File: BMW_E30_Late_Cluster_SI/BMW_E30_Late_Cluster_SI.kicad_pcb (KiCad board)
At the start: 2 copper layers, 300 x 53 mm, 115 parts, among them J1 SI LED Board, J2 Coding Plug, J5 Nexus Connector, Q11 BC327-16, Q12 BC337-25, Q13 BC337-16, Q14 BC547B, Q15 BC557B, Q17 BC337-25, Q19 BC337-25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

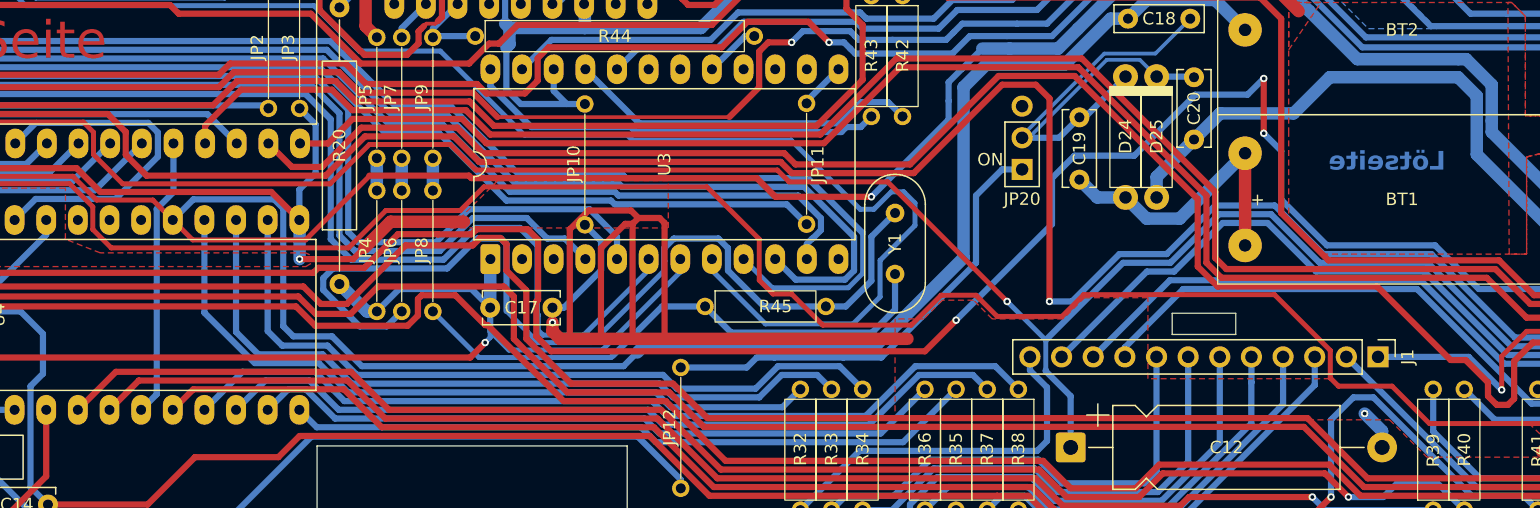
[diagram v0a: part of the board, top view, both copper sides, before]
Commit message: Readability Improvements
Organized the schematic for better readability, also made a few minor adjustments to the layout for simplicity.
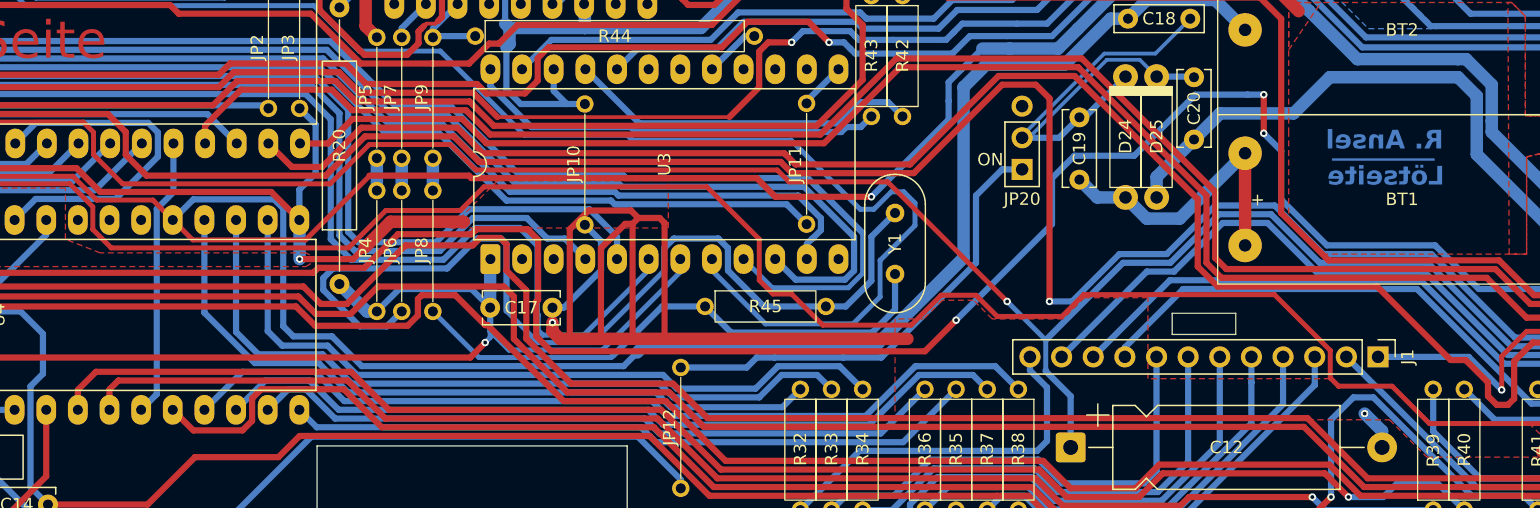
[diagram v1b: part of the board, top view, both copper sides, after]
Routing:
- net IC4_P16: track 126.0 -> 128.4 mm
- net IC4_P40: track 227.8 -> 226.0 mm
- net IC4_P14: track 112.1 -> 113.1 mm
- net IC4_P13: track 119.8 -> 120.8 mm
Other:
- board text added: "R. Ansel"
- board text added: "________"
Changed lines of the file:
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@@
 	(title_block
 		(title "BMW E30 Late Model SI Board")
+		(date "2025-12-07")
 		(rev "0")
 		(company "Reagan Ansel")
@@
 		(tags "Resistor Axial_DIN0204 series Axial Horizontal pin pitch 7.62mm 0.167W length 3.6mm diameter 1.6mm")
 		(property "Reference" "JP11"
-			(at 4.9 -0.9 90)
+			(at 4.9 0.9 90)
 			(layer "F.SilkS")
 			(effects
@@
 		(tags "Resistor Axial_DIN0204 series Axial Horizontal pin pitch 7.62mm 0.167W length 3.6mm diameter 1.6mm")
 		(property "Reference" "R45"
-			(at 5.65 0 0)
+			(at 4.85 0 0)
 			(layer "F.SilkS")
 			(effects
@@
 	)
 	(gr_text "Lötseite"
-		(at 240 153.7 0)
+		(at 235.2 154.9 0)
 		(layer "B.Cu")
 		(effects
@@
 				(bold yes)
 			)
-			(justify left bottom mirror)
+			(justify bottom mirror)
+		)
+	)
+	(gr_text "R. Ansel"
+		(at 235.1 152 0)
+		(layer "B.Cu")
+		(effects
+			(font
+				(size 1.5 1.5)
+				(thickness 0.3)
+				(bold yes)
+			)
+			(justify bottom mirror)
+		)
+	)
+	(gr_text "________"
+		(at 235 152.5 0)
+		(layer "B.Cu")
+		(effects
+			(font
+				(size 1.5 1.5)
+				(thickness 0.3)
+				(bold yes)
+			)
+			(justify bottom mirror)
 		)
 	)
@@
 	)
 	(segment
-		(start 225.4 150.6)
-		(end 225.4 146.2)
-		(width 0.5)
-		(layer "F.Cu")
-		(net 27)
-	)
-	(segment
 		(start 200.7 165.6)
 		(end 198.2 168.1)
@@
 	)
 	(segment
+		(start 225.4 150.6)
+		(end 225.4 147.5)
+		(width 0.5)
+		(layer "F.Cu")
+		(net 27)
+	)
+	(segment
 		(start 96.1 159.3)
 		(end 97.84 157.56)
@@
 	)
 	(via
-		(at 225.4 146.2)
+		(at 225.4 147.5)
 		(size 0.6)
 		(drill 0.3)
@@
 	)
 	(segment
-		(start 210.2 152.4)
-		(end 215 152.4)
+		(start 224.099 147.501)
+		(end 219.899 147.501)
 		(width 0.5)
 		(layer "B.Cu")
@@
 	)
 	(segment
+		(start 208.4 154.2)
+		(end 208.4 157.9)
+		(width 0.5)
+		(layer "B.Cu")
+		(net 27)
+	)
+	(segment
 		(start 270.6 157.7)
 		(end 268.7 159.6)
@@
 	)
 	(segment
+		(start 225.4 147.5)
+		(end 224.1 147.5)
+		(width 0.5)
+		(layer "B.Cu")
+		(net 27)
+	)
+	(segment
 		(start 273.1 154.55)
 		(end 273.1 157.9)
@@
 	)
 	(segment
-		(start 226.8 155.925908)
-		(end 226.8 152)
+		(start 210.2 152.4)
+		(end 208.4 154.2)
 		(width 0.5)
 		(layer "B.Cu")
@@
 	)
 	(segment
-		(start 257.7 163.1)
-		(end 242.65682 163.1)
+		(start 226.8 155.925908)
+		(end 226.8 152)
 		(width 0.5)
 		(layer "B.Cu")
@@
 	)
 	(segment
-		(start 208.4 154.2)
-		(end 210.2 152.4)
+		(start 257.7 163.1)
+		(end 242.65682 163.1)
 		(width 0.5)
 		(layer "B.Cu")
@@
 	)
 	(segment
-		(start 219.899 147.501)
-		(end 224.099 147.501)
+		(start 215 152.4)
+		(end 210.2 152.4)
 		(width 0.5)
 		(layer "B.Cu")
@@
 	)
 	(segment
-		(start 215 152.4)
-		(end 219.899 147.501)
-		(width 0.5)
+		(start 273.1 157.9)
+		(end 274 158.8)
+		(width 1)
 		(layer "B.Cu")
 		(net 27)
 	)
 	(segment
-		(start 208.4 157.9)
-		(end 208.4 154.2)
+		(start 219.899 147.501)
+		(end 215 152.4)
 		(width 0.5)
 		(layer "B.Cu")
@@
 	)
 	(segment
-		(start 273.1 157.9)
-		(end 274 158.8)
-		(width 1)
-		(layer "B.Cu")
-		(net 27)
-	)
-	(segment
-		(start 224.099 147.501)
-		(end 225.4 146.2)
+		(start 208.4 157.9)
+		(end 200.7 165.6)
 		(width 0.5)
 		(layer "B.Cu")
@@
 	)
 	(segment
-		(start 200.7 165.6)
-		(end 208.4 157.9)
+		(start 224.1 147.5)
+		(end 224.099 147.501)
 		(width 0.5)
 		(layer "B.Cu")
@@
 	(segment
 		(start 151.839364 170.448)
-		(end 135.092 170.448)
+		(end 133.452 170.448)
 		(width 0.5)
 		(layer "F.Cu")
@@
 	)
 	(segment
-		(start 209.282728 180.5)
-		(end 207.079728 178.297)
+		(start 229.3 179.8)
+		(end 219.4 179.8)
 		(width 0.5)
 		(layer "F.Cu")
@@
 	)
 	(segment
-		(start 176.736046 173.499)
-		(end 154.890364 173.499)
+		(start 207.079728 178.297)
+		(end 181.534046 178.297)
 		(width 0.5)
 		(layer "F.Cu")
@@
 	)
 	(segment
-		(start 207.079728 178.297)
-		(end 181.534046 178.297)
+		(start 132.74 171.16)
+		(end 132.74 172.8)
 		(width 0.5)
 		(layer "F.Cu")
@@
 	)
 	(segment
-		(start 219.4 179.8)
-		(end 218.7 180.5)
+		(start 181.534046 178.297)
+		(end 176.736046 173.499)
 		(width 0.5)
 		(layer "F.Cu")
@@
 	)
 	(segment
-		(start 229.3 179.8)
-		(end 219.4 179.8)
+		(start 209.282728 180.5)
+		(end 207.079728 178.297)
 		(width 0.5)
 		(layer "F.Cu")
@@
 	)
 	(segment
-		(start 181.534046 178.297)
-		(end 176.736046 173.499)
+		(start 176.736046 173.499)
+		(end 154.890364 173.499)
 		(width 0.5)
 		(layer "F.Cu")
@@
 	)
 	(segment
-		(start 135.092 170.448)
-		(end 132.74 172.8)
+		(start 133.452 170.448)
+		(end 132.74 171.16)
+		(width 0.5)
+		(layer "F.Cu")
+		(net 78)
+	)
+	(segment
+		(start 219.4 179.8)
+		(end 218.7 180.5)
 		(width 0.5)
 		(layer "F.Cu")
@@
 	)
 	(segment
-		(start 217.299 177.9)
-		(end 215.4 179.799)
+		(start 209.573092 179.799)
+		(end 207.370092 177.596)
 		(width 0.5)
 		(layer "F.Cu")
@@
 	)
 	(segment
-		(start 207.370092 177.596)
-		(end 181.82441 177.596)
+		(start 230.3 177.9)
+		(end 217.299 177.9)
 		(width 0.5)
 		(layer "F.Cu")
@@
 	)
 	(segment
-		(start 230.3 177.9)
-		(end 217.299 177.9)
+		(start 181.82441 177.596)
+		(end 177.02641 172.798)
 		(width 0.5)
 		(layer "F.Cu")
@@
 	)
 	(segment
-		(start 177.02641 172.798)
-		(end 155.180728 172.798)
+		(start 155.180728 172.798)
+		(end 152.129728 169.747)
 		(width 0.5)
 		(layer "F.Cu")
@@
 	)
 	(segment
-		(start 133.253 169.747)
-		(end 130.2 172.8)
+		(start 207.370092 177.596)
+		(end 181.82441 177.596)
 		(width 0.5)
 		(layer "F.Cu")
@@
 	)
 	(segment
-		(start 181.82441 177.596)
-		(end 177.02641 172.798)
+		(start 152.129728 169.747)
+		(end 131.653 169.747)
 		(width 0.5)
 		(layer "F.Cu")
@@
 	)
 	(segment
-		(start 155.180728 172.798)
-		(end 152.129728 169.747)
+		(start 177.02641 172.798)
+		(end 155.180728 172.798)
 		(width 0.5)
 		(layer "F.Cu")
@@
 	)
 	(segment
-		(start 209.573092 179.799)
-		(end 207.370092 177.596)
+		(start 131.653 169.747)
+		(end 130.2 171.2)
 		(width 0.5)
 		(layer "F.Cu")
@@
 	)
 	(segment
-		(start 152.129728 169.747)
-		(end 133.253 169.747)
+		(start 130.2 171.2)
+		(end 130.2 172.8)
+		(width 0.5)
+		(layer "F.Cu")
+		(net 79)
+	)
+	(segment
+		(start 217.299 177.9)
+		(end 215.4 179.799)
 		(width 0.5)
 		(layer "F.Cu")
@@
 	)
 	(segment
-		(start 139.471 171.149)
+		(start 139.471 174.451)
 		(end 137.82 172.8)
 		(width 0.5)
@@
 	)
 	(segment
-		(start 176.445682 174.2)
-		(end 154.6 174.2)
+		(start 154.6 174.2)
+		(end 151.549 171.149)
 		(width 0.5)
 		(layer "F.Cu")
@@
 	)
 	(segment
-		(start 154.6 174.2)
-		(end 151.549 171.149)
+		(start 181.243682 178.998)
+		(end 176.445682 174.2)
 		(width 0.5)
 		(layer "F.Cu")
@@
 	)
 	(segment
-		(start 151.549 171.149)
-		(end 139.471 171.149)
+		(start 176.445682 174.2)
+		(end 154.6 174.2)
 		(width 0.5)
 		(layer "F.Cu")
@@
 	)
 	(segment
-		(start 206.789364 178.998)
-		(end 181.243682 178.998)
+		(start 144.921819 171.149)
+		(end 144.189 171.881819)
 		(width 0.5)
 		(layer "F.Cu")
@@
 	)
 	(segment
-		(start 230.8 179.8)
-		(end 229.052 181.548)
+		(start 229.052 181.548)
+		(end 209.339364 181.548)
 		(width 0.5)
 		(layer "F.Cu")
@@
 	)
 	(segment
-		(start 229.052 181.548)
-		(end 209.339364 181.548)
+		(start 144.189 171.881819)
+		(end 144.189 173.680181)
 		(width 0.5)
 		(layer "F.Cu")
@@
 	)
 	(segment
-		(start 181.243682 178.998)
-		(end 176.445682 174.2)
+		(start 143.418181 174.451)
+		(end 139.471 174.451)
+		(width 0.5)
+		(layer "F.Cu")
+		(net 80)
+	)
+	(segment
+		(start 144.189 173.680181)
+		(end 143.418181 174.451)
+		(width 0.5)
+		(layer "F.Cu")
+		(net 80)
+	)
+	(segment
+		(start 206.789364 178.998)
+		(end 181.243682 178.998)
+		(width 0.5)
+		(layer "F.Cu")
+		(net 80)
+	)
+	(segment
+		(start 230.8 179.8)
+		(end 229.052 181.548)
+		(width 0.5)
+		(layer "F.Cu")
+		(net 80)
+	)
+	(segment
+		(start 151.549 171.149)
+		(end 144.921819 171.149)
 		(width 0.5)
 		(layer "F.Cu")

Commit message: Board Styling on SI and SI LED
Added fillets to the SI and SI_LED boards and generated the first gbr files for pricing estimation on JLC.
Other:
- outline, holes or cut-outs redrawn

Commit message: Change location of Coding Plug Connector
Updated coding plug connector to be lower so that it interfaces with the coding plug better.
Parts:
- moved J2 4.20 mm to (320.7, 146.3)
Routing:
- net GNDPWR: track 766.5 -> 774.9 mm
- net +5V: track 414.5 -> 418.7 mm
- net IC1_P4: track 318.7 -> 322.9 mm
- net IC1_P3: track 320.4 -> 324.6 mm
- net IC1_P2: track 295.8 -> 293.6 mm
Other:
- outline, holes or cut-outs redrawn
